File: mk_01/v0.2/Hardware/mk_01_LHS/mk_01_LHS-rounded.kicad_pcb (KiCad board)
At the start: 2 copper layers, 165.1 x 102.9 mm, 80 parts, among them SW1 SW_Push_Dual, U1 nice_nano

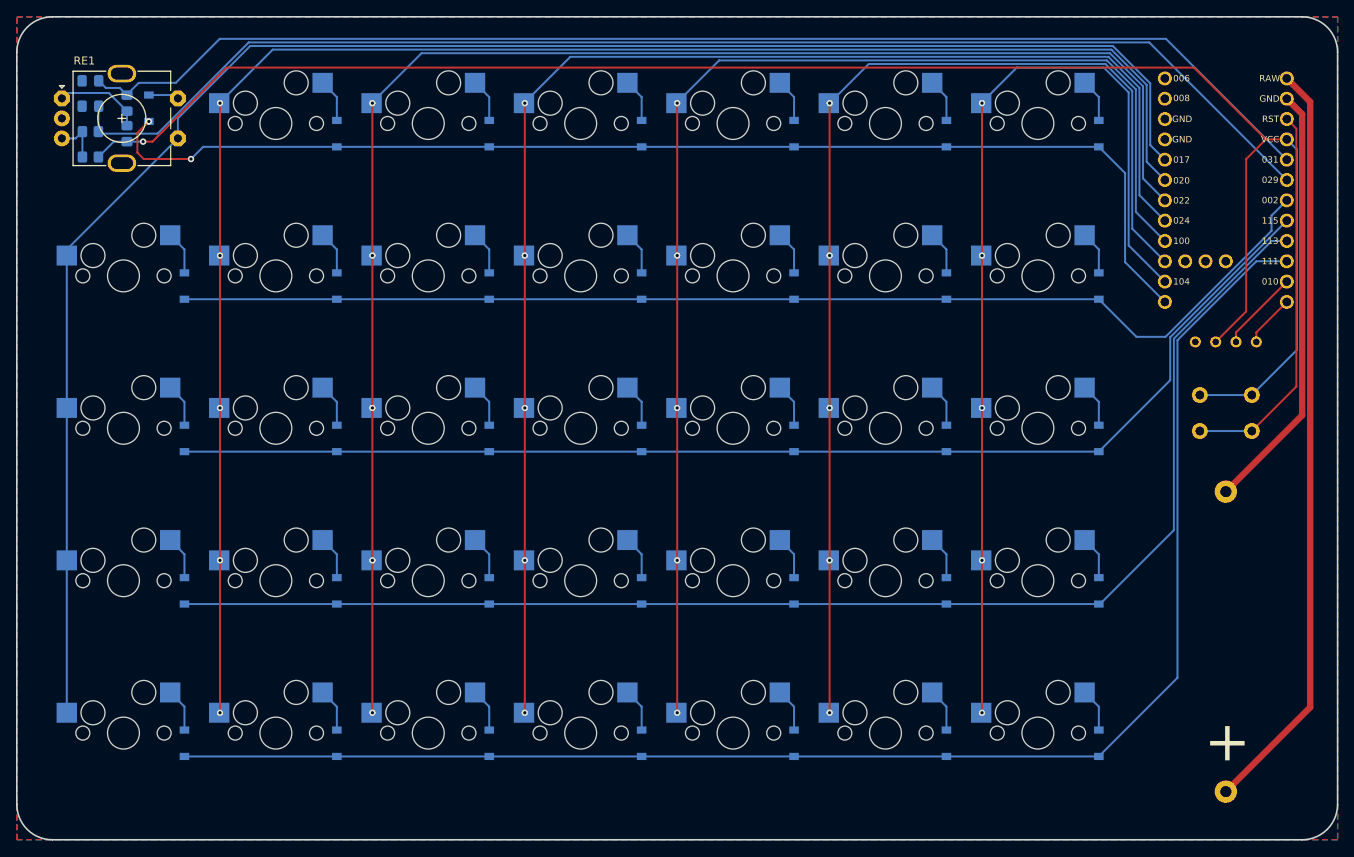
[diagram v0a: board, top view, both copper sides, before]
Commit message: Left Hand Side completion and housekeeping
The left hand side has been completed, time to start on the right hand side. I've cleared out the right hand side files, because this time I'm going to start from scratch.
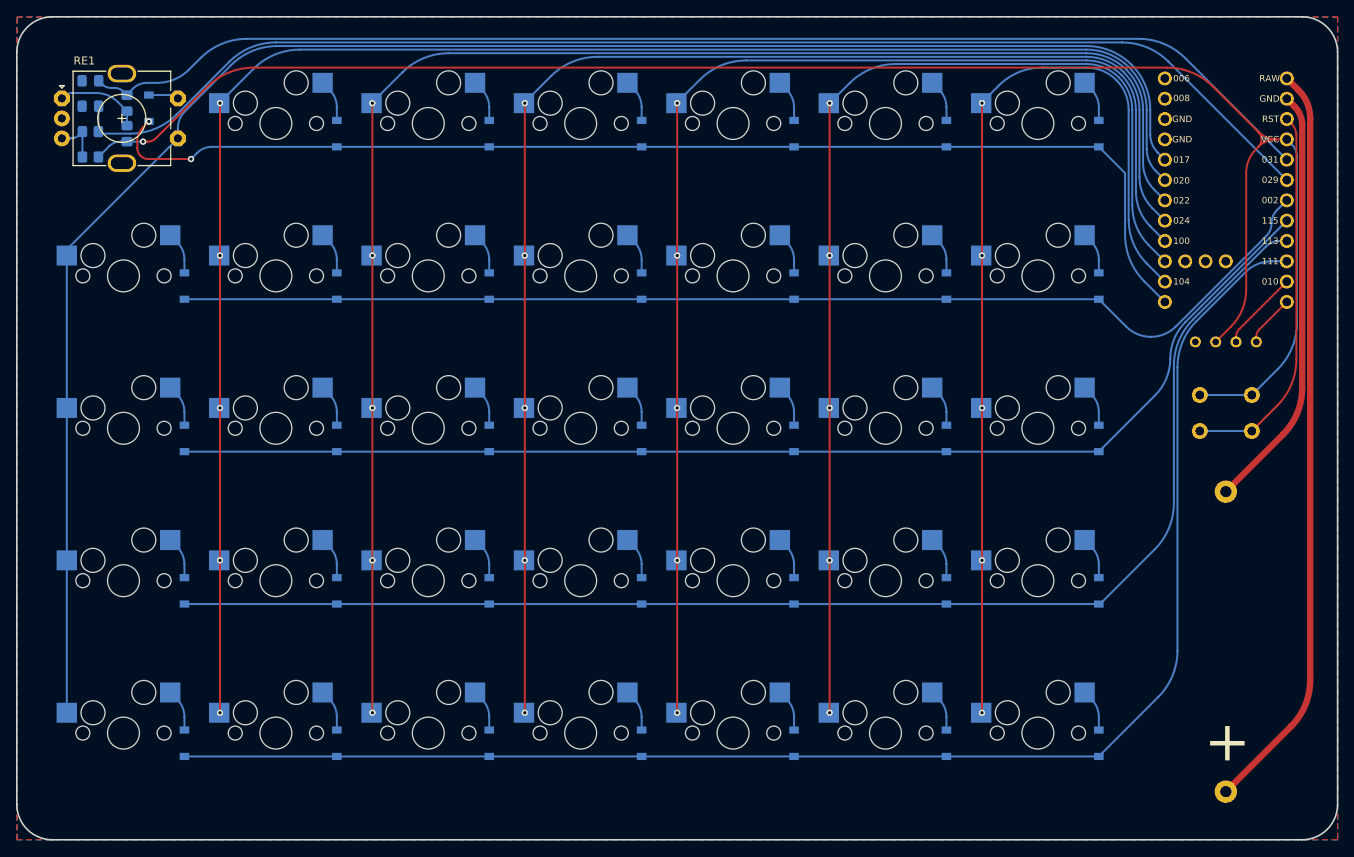
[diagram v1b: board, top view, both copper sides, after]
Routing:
- net col0: track 217.8 -> 216.3 mm
- net P0.31: track 158.5 -> 157.1 mm
- net col1: track 209.6 -> 208.3 mm
- net col2: track 192.3 -> 191.0 mm
- net col3: track 175.1 -> 173.8 mm
- net col4: track 157.8 -> 156.5 mm
- net col5: track 140.4 -> 139.2 mm
- net col6: track 123.3 -> 122.0 mm
- net P0.29: track 163.7 -> 162.5 mm
- net VCC: track 226.2 -> 227.3 mm
- net row4: track 188.2 -> 187.2 mm
- net row3: track 170.9 -> 170.0 mm
- net row2: track 153.7 -> 153.0 mm
- net row1: track 147.9 -> 147.3 mm
- net Net-(BATT1-Pad2): track 94.7 -> 94.1 mm
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
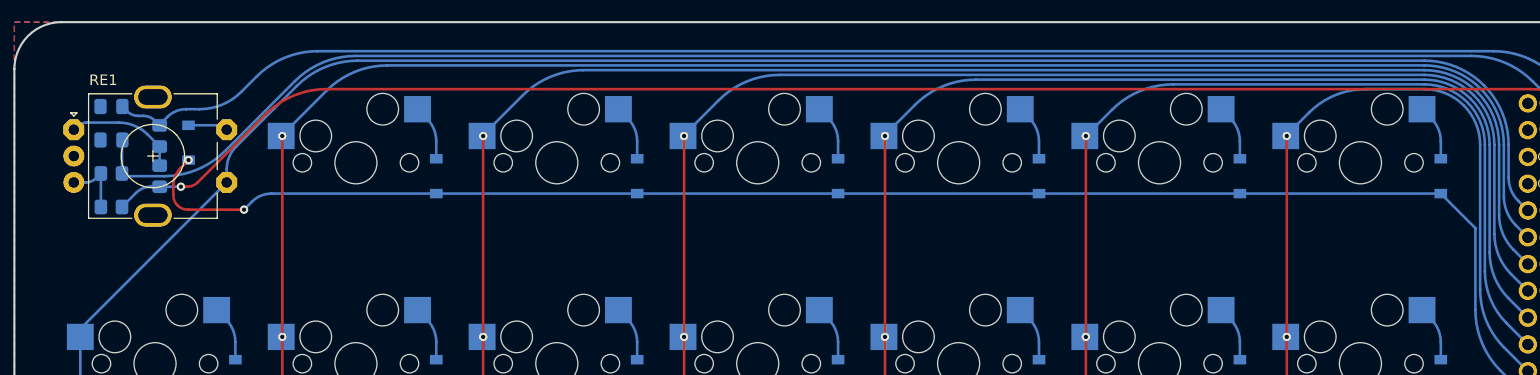
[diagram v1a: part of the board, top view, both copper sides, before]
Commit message: Right hand side mostly completed
The right hand side of the keyboard is pretty much complete, and after a final checkover of everything I think it's ready for production. I'm going to clean up the left hand side board design and schematic to match the right hand schematic style, since I based the left hand side on v0.1, and the right hand side was done from scratch.
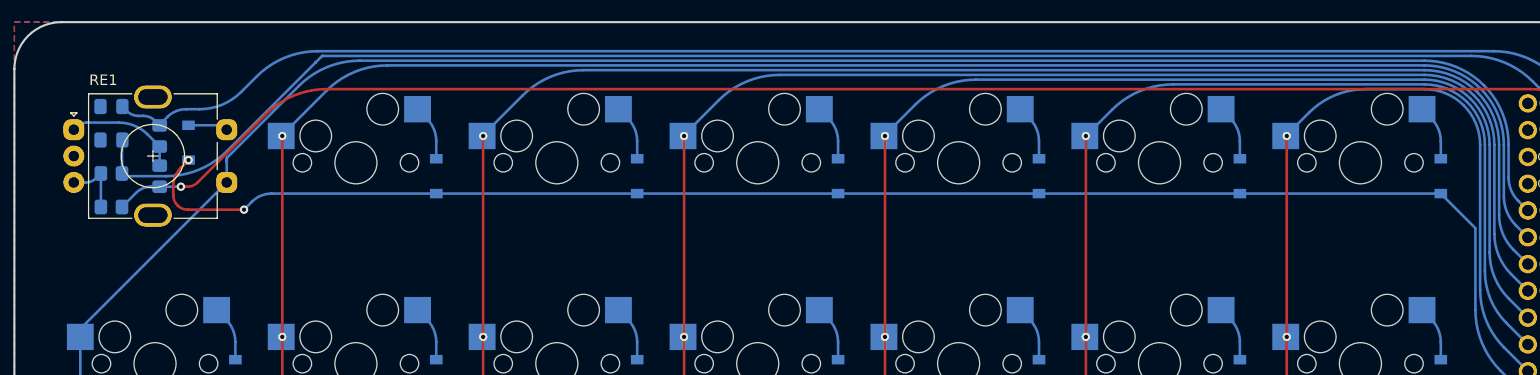
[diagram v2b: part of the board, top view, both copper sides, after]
